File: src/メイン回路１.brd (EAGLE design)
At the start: 36 parts, among them T1 一般的なトランジスタ, T2 一般的なトランジスタ, T3 一般的なトランジスタ, T4 一般的なトランジスタ

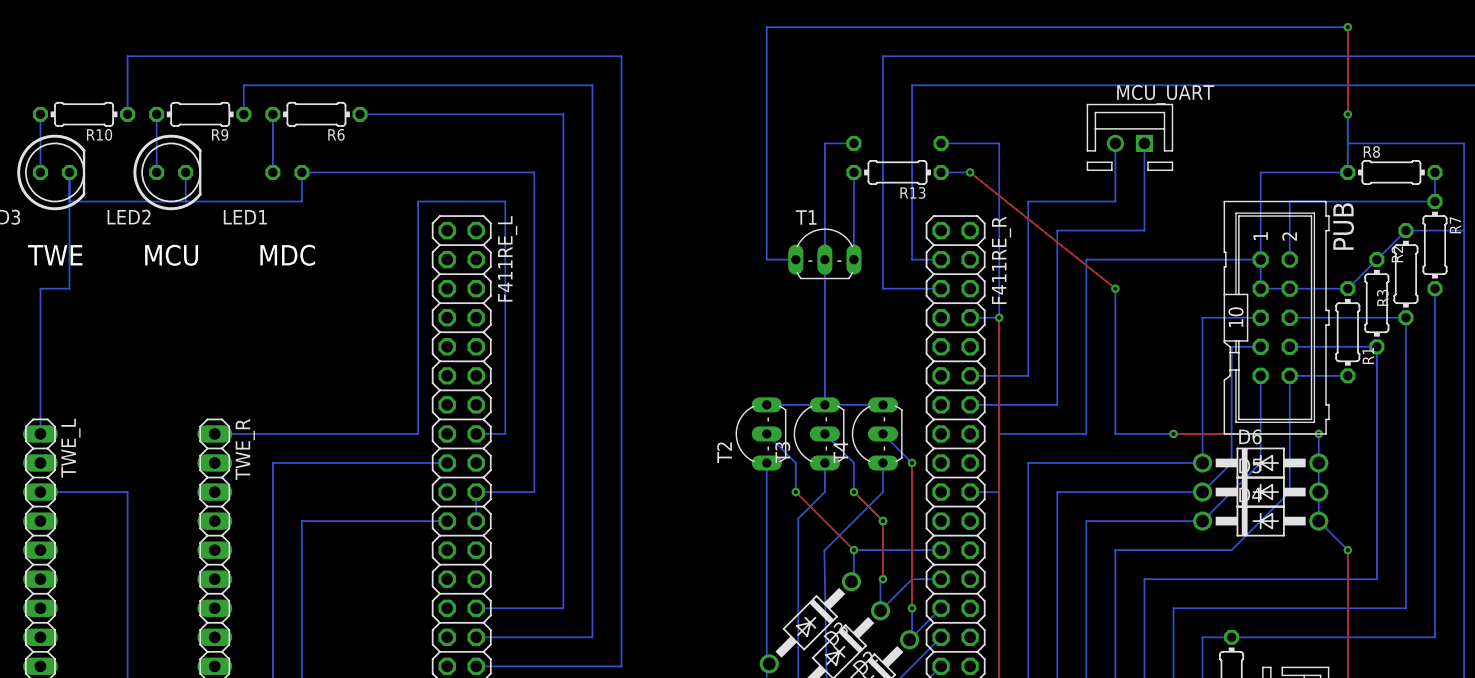
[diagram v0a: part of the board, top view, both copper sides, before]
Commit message: [fix]メイン回路1にソケット置きを追加
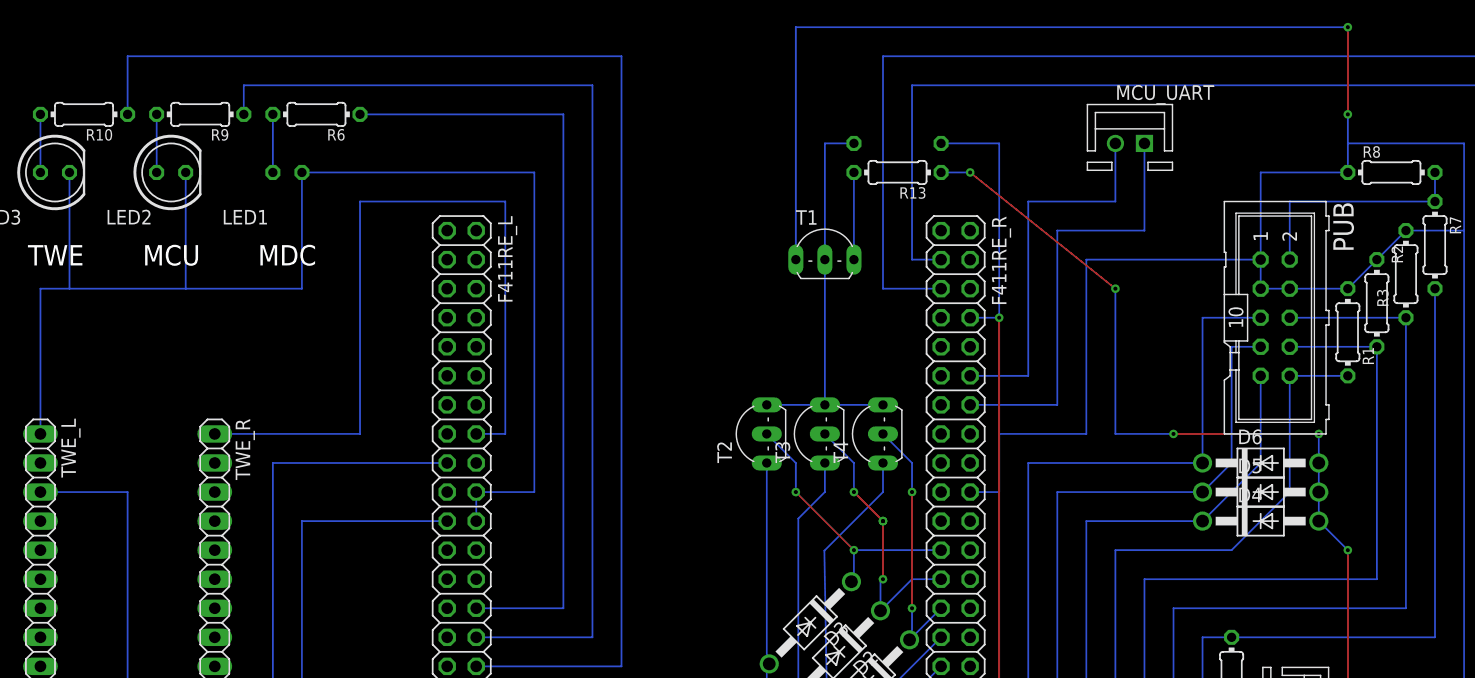
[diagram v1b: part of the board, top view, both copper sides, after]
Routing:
- net GND: track 352.6 -> 360.2 mm
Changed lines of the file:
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@@
 <contactref element="TWE_R" pad="1"/>
 <contactref element="F411RE_L" pad="16"/>
-<wire x1="15.24" y1="35.56" x2="33.02" y2="35.56" width="0.1524" layer="16"/>
-<wire x1="33.02" y1="35.56" x2="33.02" y2="55.88" width="0.1524" layer="16"/>
-<wire x1="33.02" y1="55.88" x2="40.64" y2="55.88" width="0.1524" layer="16"/>
+<wire x1="15.24" y1="35.56" x2="27.94" y2="35.56" width="0.1524" layer="16"/>
+<wire x1="27.94" y1="35.56" x2="27.94" y2="55.88" width="0.1524" layer="16"/>
+<wire x1="27.94" y1="55.88" x2="40.64" y2="55.88" width="0.1524" layer="16"/>
 <wire x1="40.64" y1="55.88" x2="40.64" y2="35.56" width="0.1524" layer="16"/>
 <wire x1="40.64" y1="35.56" x2="38.1" y2="35.56" width="0.1524" layer="16"/>
@@
 <contactref element="PUB" pad="4"/>
 <contactref element="PUB" pad="3"/>
-<wire x1="114.3" y1="48.26" x2="119.38" y2="53.34" width="0.1524" layer="16"/>
 <wire x1="109.22" y1="48.26" x2="106.68" y2="48.26" width="0.1524" layer="16"/>
 <wire x1="106.68" y1="48.26" x2="106.68" y2="50.8" width="0.1524" layer="16"/>
@@
 <wire x1="0" y1="48.26" x2="2.54" y2="48.26" width="0.1524" layer="16"/>
 <wire x1="2.54" y1="48.26" x2="2.54" y2="58.42" width="0.1524" layer="16"/>
-<wire x1="2.54" y1="58.42" x2="2.54" y2="55.88" width="0.1524" layer="16"/>
-<wire x1="2.54" y1="55.88" x2="12.7" y2="55.88" width="0.1524" layer="16"/>
-<wire x1="12.7" y1="58.42" x2="12.7" y2="55.88" width="0.1524" layer="16"/>
-<wire x1="12.7" y1="55.88" x2="22.86" y2="55.88" width="0.1524" layer="16"/>
-<wire x1="22.86" y1="55.88" x2="22.86" y2="58.42" width="0.1524" layer="16"/>
+<wire x1="2.54" y1="48.26" x2="12.7" y2="48.26" width="0.1524" layer="16"/>
+<wire x1="12.7" y1="58.42" x2="12.7" y2="48.26" width="0.1524" layer="16"/>
+<wire x1="12.7" y1="48.26" x2="22.86" y2="48.26" width="0.1524" layer="16"/>
+<wire x1="22.86" y1="48.26" x2="22.86" y2="58.42" width="0.1524" layer="16"/>
 <wire x1="124.46" y1="53.34" x2="119.38" y2="53.34" width="0.1524" layer="16"/>
 <wire x1="114.3" y1="58.42" x2="114.3" y2="60.96" width="0.1524" layer="16"/>
@@
 <wire x1="124.46" y1="12.7" x2="124.46" y2="53.34" width="0.1524" layer="16"/>
 <contactref element="T1" pad="E"/>
-<wire x1="66.04" y1="50.8" x2="63.5" y2="50.8" width="0.1524" layer="16"/>
-<wire x1="63.5" y1="50.8" x2="63.5" y2="71.12" width="0.1524" layer="16"/>
-<wire x1="114.3" y1="71.12" x2="63.5" y2="71.12" width="0.1524" layer="16"/>
+<wire x1="66.04" y1="50.8" x2="66.04" y2="71.12" width="0.1524" layer="16"/>
+<wire x1="114.3" y1="71.12" x2="66.04" y2="71.12" width="0.1524" layer="16"/>
 <via x="114.3" y="71.12" extent="1-16" drill="0.35"/>
 <wire x1="114.3" y1="71.12" x2="114.3" y2="63.5" width="0.1524" layer="1"/>
 <via x="114.3" y="63.5" extent="1-16" drill="0.35"/>
 <wire x1="114.3" y1="63.5" x2="114.3" y2="60.96" width="0.1524" layer="16"/>
-<wire x1="119.38" y1="53.34" x2="116.84" y2="50.8" width="0" layer="19" extent="1-1"/>
+<wire x1="114.3" y1="48.26" x2="116.84" y2="50.8" width="0.1524" layer="16"/>
+<wire x1="116.84" y1="50.8" x2="119.38" y2="53.34" width="0.1524" layer="16"/>
 <wire x1="38.1" y1="30.48" x2="66.04" y2="50.8" width="0" layer="19" extent="1-1"/>
 </signal>
@@
 <wire x1="75.9821" y1="17.5621" x2="76.2" y2="17.78" width="0.1524" layer="16"/>
 <wire x1="76.2" y1="17.78" x2="78.74" y2="20.32" width="0.1524" layer="16"/>
-<wire x1="73.66" y1="35.56" x2="76.2" y2="33.02" width="0.1524" layer="16"/>
-<via x="76.2" y="33.02" extent="1-16" drill="0.35"/>
-<wire x1="76.2" y1="33.02" x2="76.2" y2="20.32" width="0.1524" layer="1"/>
+<via x="76.2" y="30.48" extent="1-16" drill="0.35"/>
+<wire x1="76.2" y1="30.48" x2="76.2" y2="20.32" width="0.1524" layer="1"/>
 <via x="76.2" y="20.32" extent="1-16" drill="0.35"/>
 <wire x1="76.2" y1="20.32" x2="76.2" y2="17.78" width="0.1524" layer="16"/>
+<wire x1="73.66" y1="35.56" x2="76.2" y2="33.02" width="0.1524" layer="16"/>
+<wire x1="76.2" y1="33.02" x2="76.2" y2="30.48" width="0.1524" layer="16"/>
 </signal>
 <signal name="SDA">
@@
 <wire x1="68.58" y1="60.96" x2="71.12" y2="60.96" width="0.1524" layer="16"/>
 <wire x1="68.58" y1="50.8" x2="68.58" y2="38.1" width="0.1524" layer="16"/>
-<wire x1="73.66" y1="38.1" x2="63.5" y2="38.1" width="0.1524" layer="16"/>
-<wire x1="63.5" y1="38.1" x2="68.58" y2="38.1" width="0" layer="19" extent="1-1"/>
+<wire x1="63.5" y1="38.1" x2="68.58" y2="38.1" width="0.1524" layer="16"/>
+<wire x1="68.58" y1="38.1" x2="73.66" y2="38.1" width="0.1524" layer="16"/>
 </signal>
 <signal name="N$4">

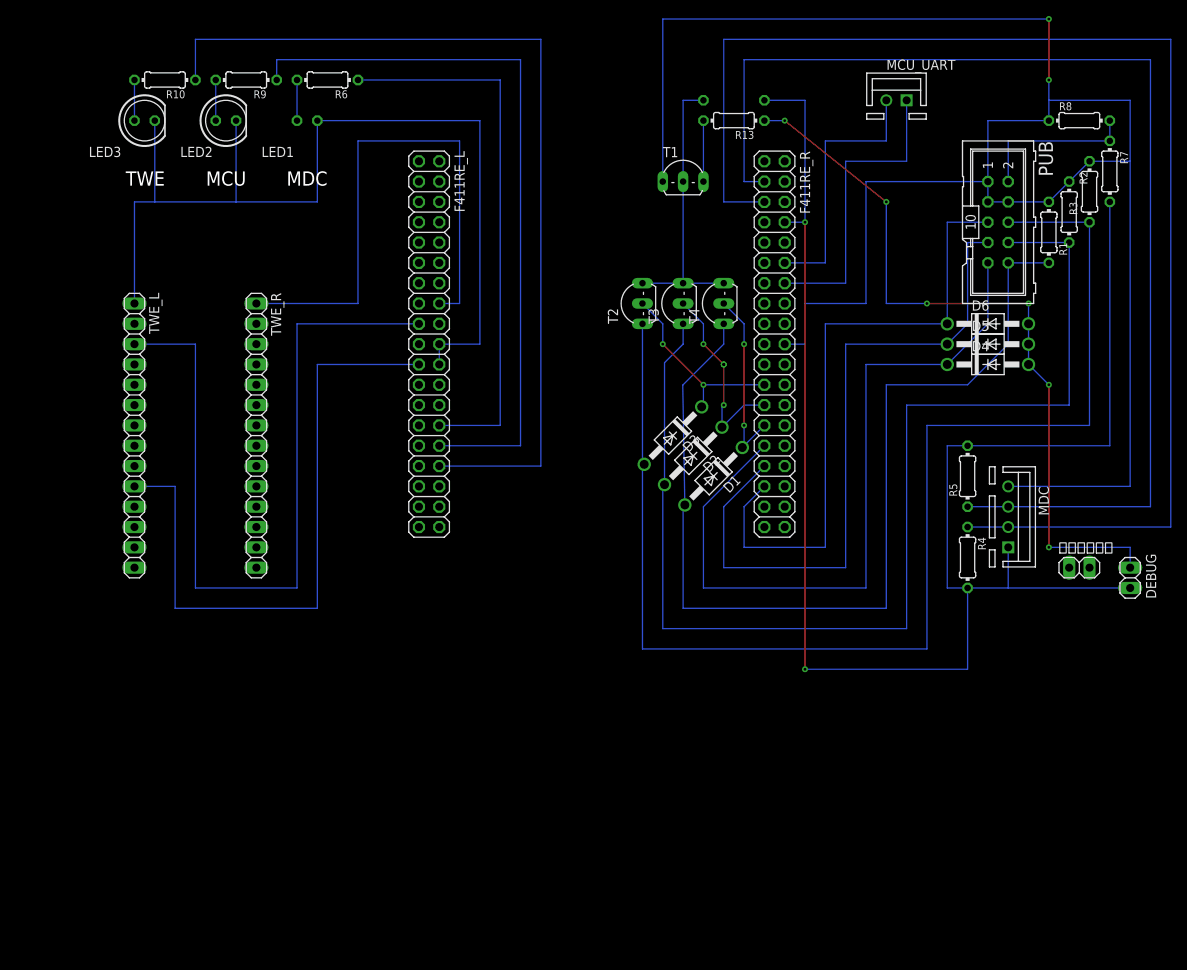
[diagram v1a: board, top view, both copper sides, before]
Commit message: 暴走対策機能付き非常停止スイッチの回路のガバを修復
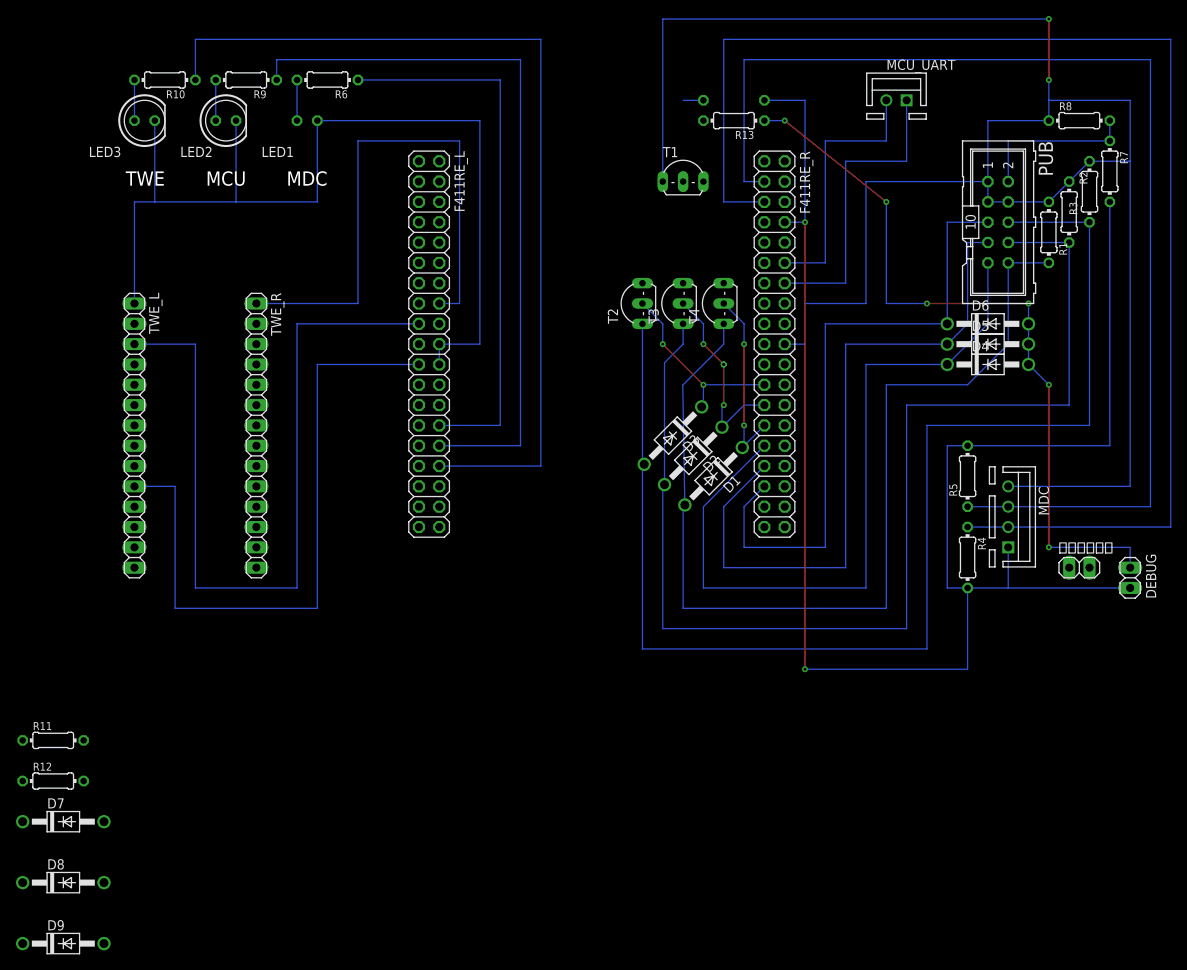
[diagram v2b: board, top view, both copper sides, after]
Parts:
- added D7, D8, D9: 1N4004, diode:DO41-10
- added R11, R12: 10k, rcl:0204/7
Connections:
- new net N$5: D8.A, R11.1, T3.B
- new net N$6: D9.A, R12.1, T2.B
- new net N$7: D7.C, D8.C, D9.C, T1.C
- net U5V: now also R11.2, R12.2
- net ZM: now also D7.A; no longer T1.C, T2.B, T3.B
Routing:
- net ZM: track 35.6 -> 2.54 mm
- net N$4: track 7.62 -> 0.00 mm
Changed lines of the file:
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@@
 <attribute name="VALUE" x="115.57" y="-0.635" size="1.27" layer="27"/>
+</element>
+<element name="R11" library="rcl" library_urn="urn:adsk.eagle:library:334" package="0204/7" package3d_urn="urn:adsk.eagle:package:23498/2" value="10k" x="-10.16" y="-19.05" smashed="yes">
+<attribute name="NAME" x="-12.7" y="-17.7546" size="0.9906" layer="25" ratio="10"/>
+<attribute name="POPULARITY" value="79" x="-10.16" y="-19.05" size="1.778" layer="27" display="off"/>
+<attribute name="SPICEPREFIX" value="R" x="-10.16" y="-19.05" size="1.778" layer="27" display="off"/>
+<attribute name="VALUE" x="-11.7856" y="-19.5326" size="0.9906" layer="27" ratio="10"/>
+</element>
+<element name="R12" library="rcl" library_urn="urn:adsk.eagle:library:334" package="0204/7" package3d_urn="urn:adsk.eagle:package:23498/2" value="10k" x="-10.16" y="-24.13" smashed="yes">
+<attribute name="NAME" x="-12.7" y="-22.8346" size="0.9906" layer="25" ratio="10"/>
+<attribute name="POPULARITY" value="79" x="-10.16" y="-24.13" size="1.778" layer="27" display="off"/>
+<attribute name="SPICEPREFIX" value="R" x="-10.16" y="-24.13" size="1.778" layer="27" display="off"/>
+<attribute name="VALUE" x="-11.7856" y="-24.6126" size="0.9906" layer="27" ratio="10"/>
+</element>
+<element name="D7" library="diode" library_urn="urn:adsk.eagle:library:210" package="DO41-10" package3d_urn="urn:adsk.eagle:package:43336/1" value="1N4004" x="-8.89" y="-29.21" smashed="yes">
+<attribute name="NAME" x="-10.922" y="-27.559" size="1.27" layer="25" ratio="10"/>
+<attribute name="POPULARITY" value="82" x="-8.89" y="-29.21" size="1.778" layer="27" display="off"/>
+<attribute name="VALUE" x="-10.922" y="-32.004" size="1.27" layer="27" ratio="10"/>
+</element>
+<element name="D8" library="diode" library_urn="urn:adsk.eagle:library:210" package="DO41-10" package3d_urn="urn:adsk.eagle:package:43336/1" value="1N4004" x="-8.89" y="-36.83" smashed="yes">
+<attribute name="NAME" x="-10.922" y="-35.179" size="1.27" layer="25" ratio="10"/>
+<attribute name="POPULARITY" value="82" x="-8.89" y="-36.83" size="1.778" layer="27" display="off"/>
+<attribute name="VALUE" x="-10.922" y="-39.624" size="1.27" layer="27" ratio="10"/>
+</element>
+<element name="D9" library="diode" library_urn="urn:adsk.eagle:library:210" package="DO41-10" package3d_urn="urn:adsk.eagle:package:43336/1" value="1N4004" x="-8.89" y="-44.45" smashed="yes">
+<attribute name="NAME" x="-10.922" y="-42.799" size="1.27" layer="25" ratio="10"/>
+<attribute name="POPULARITY" value="82" x="-8.89" y="-44.45" size="1.778" layer="27" display="off"/>
+<attribute name="VALUE" x="-10.922" y="-47.244" size="1.27" layer="27" ratio="10"/>
 </element>
 </elements>
@@
 <wire x1="78.74" y1="60.96" x2="83.82" y2="60.96" width="0.1524" layer="16"/>
 <wire x1="83.82" y1="60.96" x2="83.82" y2="45.72" width="0.1524" layer="16"/>
+<contactref element="R11" pad="2"/>
+<contactref element="R12" pad="2"/>
+<wire x1="-6.35" y1="-19.05" x2="83.82" y2="-10.16" width="0" layer="19" extent="1-1"/>
+<wire x1="-6.35" y1="-24.13" x2="-6.35" y2="-19.05" width="0" layer="19" extent="1-1"/>
 </signal>
 <signal name="3V">
@@
 </signal>
 <signal name="ZM">
-<contactref element="T1" pad="C"/>
+<contactref element="T4" pad="B"/>
 <contactref element="R14" pad="1"/>
-<contactref element="T2" pad="B"/>
-<contactref element="T3" pad="B"/>
-<contactref element="T4" pad="B"/>
-<wire x1="68.58" y1="50.8" x2="68.58" y2="60.96" width="0.1524" layer="16"/>
 <wire x1="68.58" y1="60.96" x2="71.12" y2="60.96" width="0.1524" layer="16"/>
-<wire x1="68.58" y1="50.8" x2="68.58" y2="38.1" width="0.1524" layer="16"/>
-<wire x1="63.5" y1="38.1" x2="68.58" y2="38.1" width="0.1524" layer="16"/>
-<wire x1="68.58" y1="38.1" x2="73.66" y2="38.1" width="0.1524" layer="16"/>
-</signal>
-<signal name="N$4">
-<contactref element="R13" pad="2"/>
-<contactref element="T1" pad="B"/>
-<wire x1="71.12" y1="58.42" x2="71.12" y2="50.8" width="0.1524" layer="16"/>
+<contactref element="D7" pad="A"/>
+<wire x1="73.66" y1="38.1" x2="71.12" y2="60.96" width="0" layer="19" extent="1-1"/>
+<wire x1="-3.81" y1="-29.21" x2="73.66" y2="38.1" width="0" layer="19" extent="1-1"/>
 </signal>
 <signal name="N$8">
@@
 <wire x1="63.5" y1="33.02" x2="63.5" y2="15.24" width="0.1524" layer="16"/>
 </signal>
+<signal name="N$6">
+<contactref element="T2" pad="B"/>
+<contactref element="R12" pad="1"/>
+<contactref element="D9" pad="A"/>
+<wire x1="-13.97" y1="-24.13" x2="63.5" y2="38.1" width="0" layer="19" extent="1-1"/>
+<wire x1="-3.81" y1="-44.45" x2="-13.97" y2="-24.13" width="0" layer="19" extent="1-1"/>
+</signal>
+<signal name="N$5">
+<contactref element="R11" pad="1"/>
+<contactref element="T3" pad="B"/>
+<contactref element="D8" pad="A"/>
+<wire x1="-13.97" y1="-19.05" x2="68.58" y2="38.1" width="0" layer="19" extent="1-1"/>
+<wire x1="-3.81" y1="-36.83" x2="-13.97" y2="-19.05" width="0" layer="19" extent="1-1"/>
+</signal>
+<signal name="N$4">
+<contactref element="T1" pad="B"/>
+<contactref element="R13" pad="2"/>
+<wire x1="71.12" y1="50.8" x2="71.12" y2="58.42" width="0" layer="19" extent="1-1"/>
+</signal>
+<signal name="N$7">
+<contactref element="D7" pad="C"/>
+<contactref element="D9" pad="C"/>
+<contactref element="D8" pad="C"/>
+<contactref element="T1" pad="C"/>
+<wire x1="-13.97" y1="-29.21" x2="68.58" y2="50.8" width="0" layer="19" extent="1-1"/>
+<wire x1="-13.97" y1="-36.83" x2="-13.97" y2="-29.21" width="0" layer="19" extent="1-1"/>
+<wire x1="-13.97" y1="-44.45" x2="-13.97" y2="-36.83" width="0" layer="19" extent="1-1"/>
+</signal>
 </signals>
